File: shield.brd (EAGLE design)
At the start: 35.7 x 44.6 mm, 40 parts, among them Q1 BSS138, Q2 BSS138, Q3 BSS138, Q4 BSS138, Q5 BSS138, Q6 BSS138, Q7 BSS138, Q8 BSS138

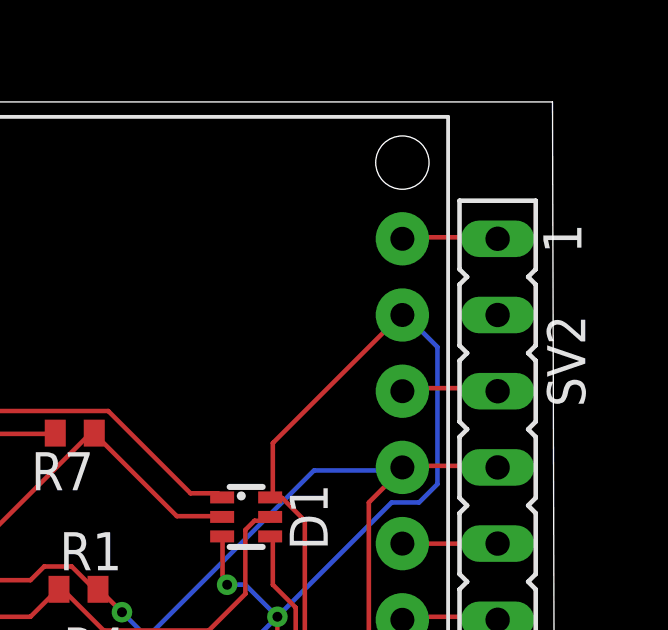
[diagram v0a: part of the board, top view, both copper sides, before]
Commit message: fixing ground line
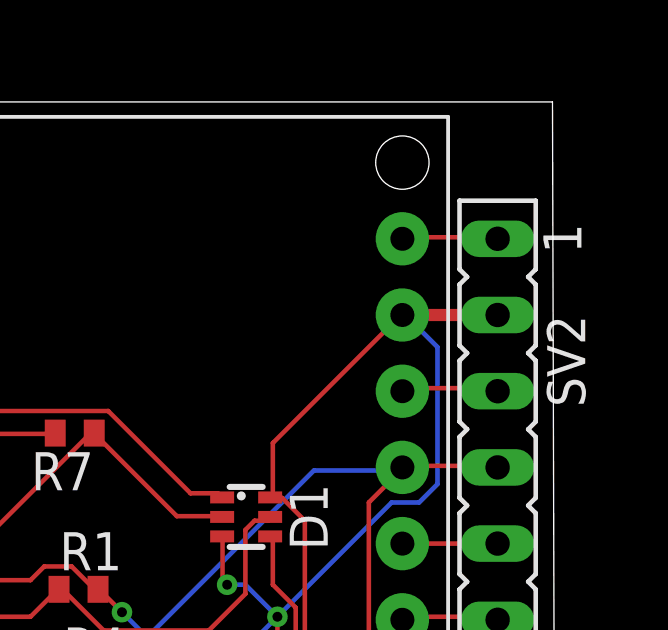
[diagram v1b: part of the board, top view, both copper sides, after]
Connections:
- removed net N$15: SV2.2
- net N$1: now also SV2.2
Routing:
- net N$1: track 76.5 -> 79.5 mm
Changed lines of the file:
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@@
 </signal>
 <signal name="N$1">
-<contactref element="U$1" pad="GND1"/>
 <contactref element="D1" pad="3"/>
 <contactref element="D1" pad="6"/>
@@
 <wire x1="43.2816" y1="45.72" x2="44.3484" y2="44.6532" width="0.1524" layer="16"/>
 <wire x1="39.0144" y1="33.3756" x2="38.9" y2="33.289" width="0.1524" layer="1"/>
-<wire x1="43.2816" y1="45.72" x2="43.18" y2="45.72" width="0.1524" layer="16"/>
 <wire x1="37.1856" y1="36.8808" x2="37.1856" y2="38.2524" width="0.1524" layer="1"/>
 <wire x1="37.338" y1="36.7284" x2="37.1856" y2="36.8808" width="0.1524" layer="1"/>
@@
 <wire x1="43.1292" y1="45.72" x2="38.862" y2="41.4528" width="0.1524" layer="1"/>
 <wire x1="38.862" y1="39.7764" x2="38.773" y2="39.639" width="0.1524" layer="1"/>
-<wire x1="43.1292" y1="45.72" x2="43.18" y2="45.72" width="0.1524" layer="1"/>
 <via x="39.0144" y="35.6616" extent="1-16" drill="0.3302"/>
 <via x="37.338" y="36.7284" extent="1-16" drill="0.3302"/>
 <via x="38.1" y="31.3944" extent="1-16" drill="0.3302"/>
 <via x="36.7284" y="25.146" extent="1-16" drill="0.3302"/>
+<contactref element="U$1" pad="GND1"/>
+<contactref element="SV2" pad="2"/>
+<wire x1="46.355" y1="45.72" x2="43.18" y2="45.72" width="0.4064" layer="1"/>
+<wire x1="43.1292" y1="45.72" x2="43.18" y2="45.72" width="0" layer="19" extent="1-1"/>
+<wire x1="43.2816" y1="45.72" x2="43.18" y2="45.72" width="0" layer="19" extent="16-16"/>
 </signal>
 <signal name="N$9">
@@
 <wire x1="43.2816" y1="43.2816" x2="43.18" y2="43.18" width="0.1524" layer="1"/>
 </signal>
-<signal name="N$15">
-<contactref element="SV2" pad="2"/>
-</signal>
 <signal name="N$16">

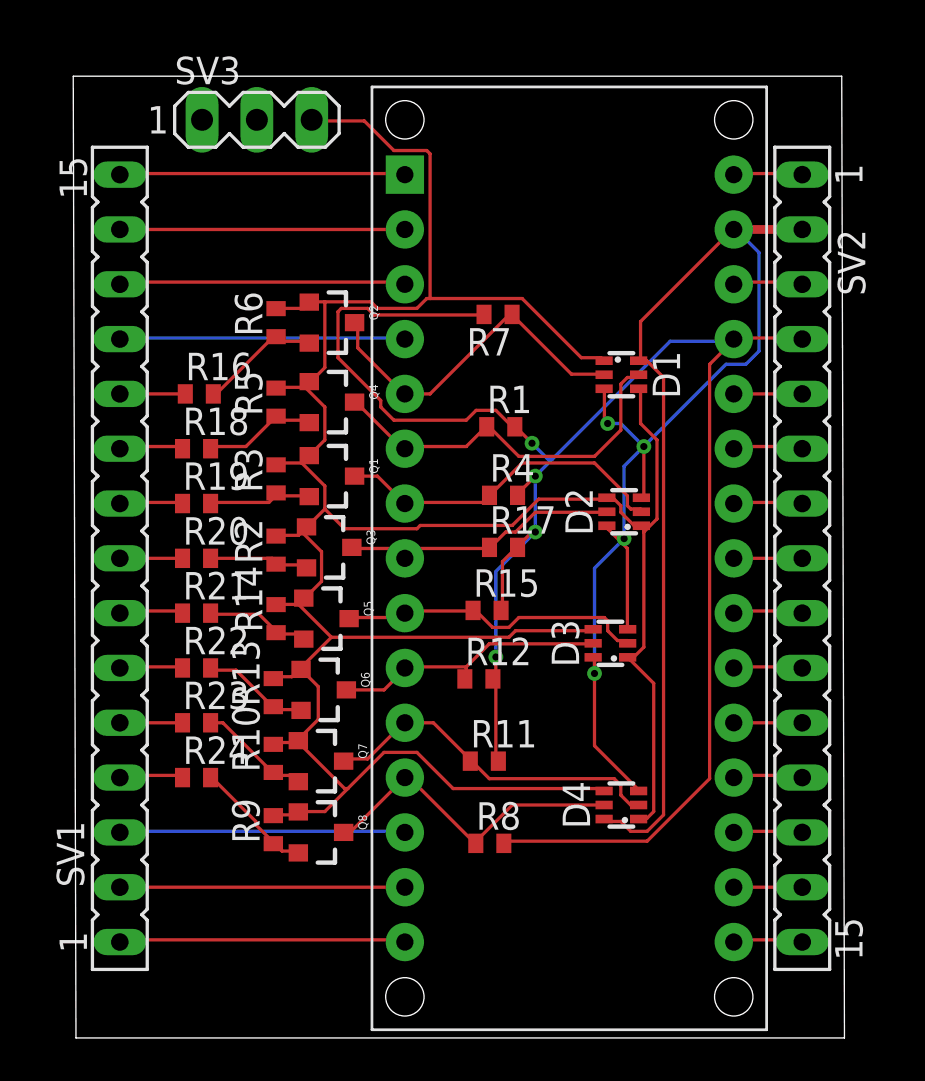
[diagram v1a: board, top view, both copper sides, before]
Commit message: optimizing board layout using reverse side for mounting
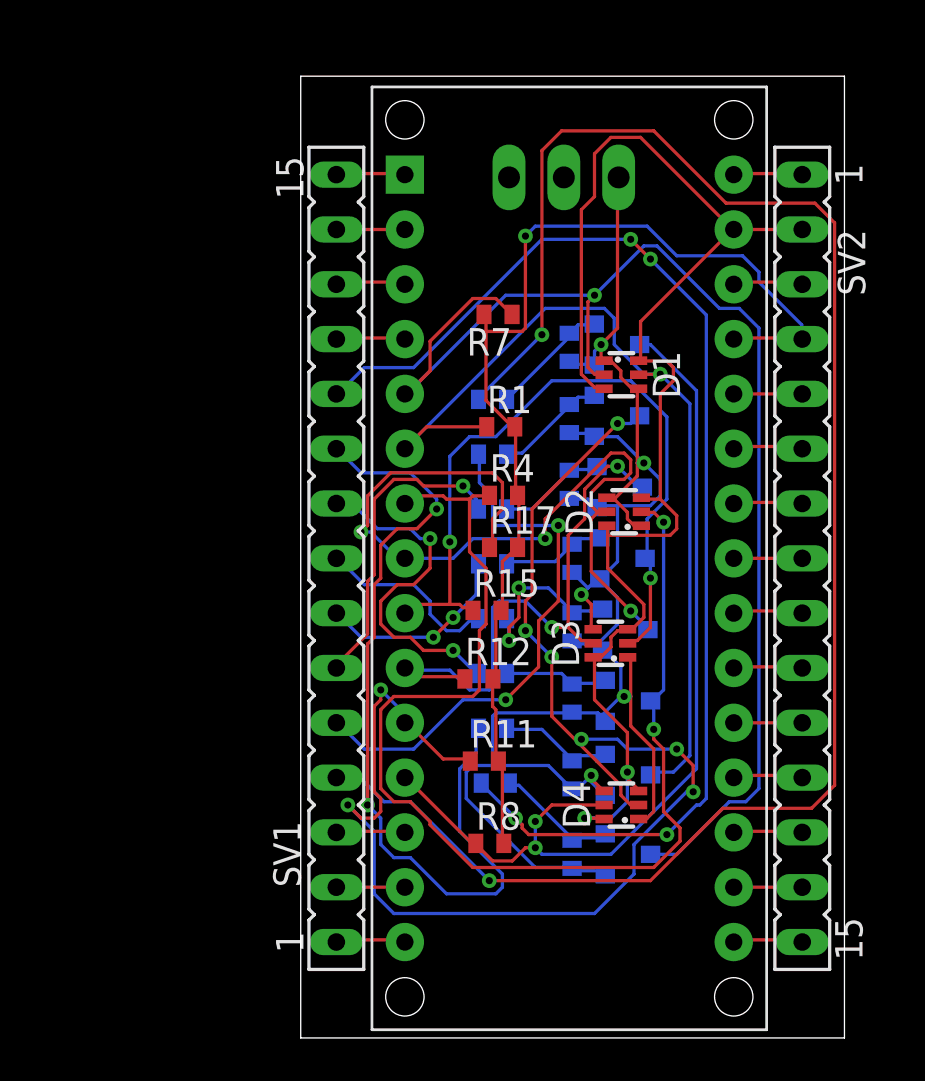
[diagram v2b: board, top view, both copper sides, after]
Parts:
- moved Q2 28.2 mm to (38.2, 16.8), flipped to the bottom, turned to 90 degrees
- moved R6 28.2 mm to (35.7, 16.8), flipped to the bottom, turned to 270 degrees
- moved Q8 26.4 mm to (37.7, 40.4), flipped to the bottom, turned to 90 degrees
- moved R9 26.2 mm to (35.6, 40.3), flipped to the bottom, turned to 270 degrees
- moved R16 22.7 mm to (32.1, 20.1), flipped to the bottom, turned to 180 degrees
- moved R24 22.3 mm to (32.0, 37.8), flipped to the bottom, turned to 180 degrees
- moved Q4 22.1 mm to (38.2, 20.4), flipped to the bottom, turned to 90 degrees
- moved R5 22.1 mm to (35.7, 20.4), flipped to the bottom, turned to 270 degrees
- moved Q7 21.1 mm to (37.7, 37.1), flipped to the bottom, turned to 90 degrees
- moved R10 20.9 mm to (35.6, 37.0), flipped to the bottom, turned to 270 degrees
- moved R18 18.9 mm to (32.0, 22.6), flipped to the bottom, turned to 180 degrees
- moved R23 18.5 mm to (32.0, 35.3), flipped to the bottom, turned to 180 degrees
- moved Q1 17.2 mm to (38.2, 23.9), flipped to the bottom, turned to 90 degrees
- moved R3 17.1 mm to (35.7, 24.0), flipped to the bottom, turned to 270 degrees
- moved R13 16.8 mm to (35.6, 33.9), flipped to the bottom, turned to 270 degrees
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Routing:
- net N$28: track 3.01 -> 81.4 mm, vias 0 -> 2
- net N$13: track 3.03 -> 56.2 mm, vias 0 -> 4
- net LV: track 135.5 -> 84.9 mm, vias 0 -> 5
- net HV8: track 16.3 -> 66.6 mm, vias 0 -> 8
- net HV2: track 16.2 -> 60.7 mm, vias 0 -> 1
- net HV4: track 15.8 -> 54.9 mm, vias 0 -> 2
- net HV: track 88.0 -> 51.3 mm, vias 4 -> 1
- net N$22: track 3.01 -> 39.0 mm, vias 0 -> 2
- net HV9: track 15.2 -> 42.9 mm, vias 0 -> 2
- net HV5: track 12.9 -> 38.5 mm, vias 0 -> 3
- net HV3: track 17.9 -> 42.2 mm, vias 0 -> 1
- net N$27: track 2.91 -> 24.9 mm, vias 0 -> 2
- net HV6: track 14.4 -> 34.2 mm, vias 0 -> 2
- net HV7: track 12.9 -> 27.1 mm, vias 0 -> 2
- net N$1: track 79.5 -> 65.4 mm, vias 4 -> 2
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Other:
- board size 35.7 x 44.6 mm -> 25.2 x 44.6 mm

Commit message: reducing size dramatically
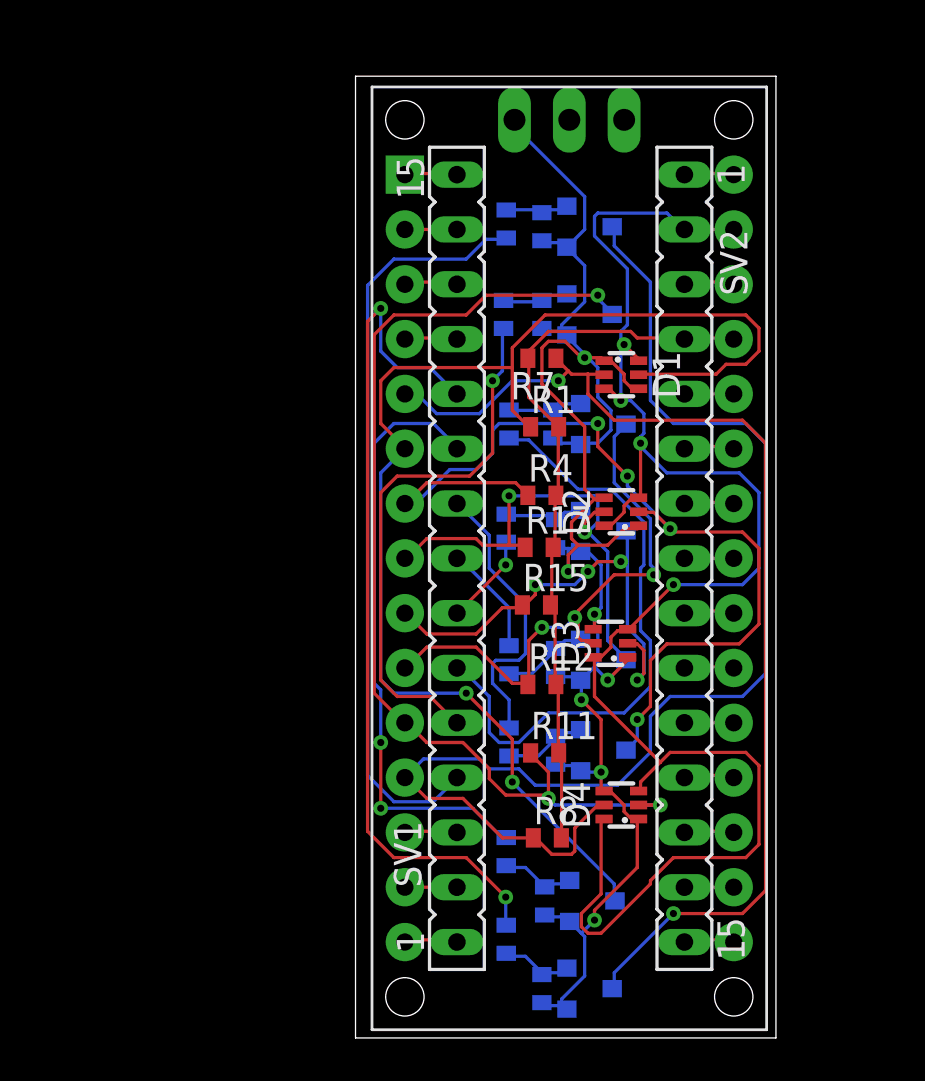
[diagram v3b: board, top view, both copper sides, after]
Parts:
- moved R24 8.15 mm to (32.6, 46.0), turned to 90 degrees
- moved R16 7.26 mm to (32.6, 12.8), turned to 270 degrees
- moved R23 6.50 mm to (32.5, 41.8), turned to 90 degrees
- moved Q2 6.47 mm to (36.4, 10.5)
- moved R6 6.38 mm to (34.3, 10.5)
- moved Q4 6.07 mm to (36.6, 14.6)
- moved R5 5.98 mm to (34.4, 14.6)
- moved R18 5.75 mm to (32.6, 16.9), turned to 270 degrees
- moved R9 5.73 mm to (34.3, 45.8)
- moved Q8 5.61 mm to (36.4, 45.8)
- moved SV1 5.59 mm to (30.4, 30.5)
- moved SV2 5.46 mm to (40.9, 30.5)
- moved R10 4.99 mm to (34.3, 41.8)
- moved Q7 4.87 mm to (36.4, 41.8)
- moved R22 4.01 mm to (32.8, 36.7), turned to 90 degrees
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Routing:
- net N$28: track 81.4 -> 35.2 mm, vias 2 -> 0
- net HV3: track 42.2 -> 61.3 mm, vias 1 -> 2
- net HV8: track 66.6 -> 47.9 mm, vias 8 -> 3
- net HV: track 51.3 -> 33.6 mm, vias 1 -> 0
- net N$13: track 56.2 -> 39.8 mm, vias 4 -> 2
- net HV5: track 38.5 -> 22.6 mm, vias 3 -> 2
- net HV9: track 42.9 -> 58.6 mm, vias 2 -> 0
- net N$26: track 14.7 -> 28.3 mm, vias 1 -> 0
- net N$1: track 65.4 -> 77.8 mm, vias 2 -> 4
- net HV6: track 34.2 -> 22.2 mm, vias 2 -> 4
- net HV4: track 54.9 -> 43.8 mm, vias 2 -> 4
- net N$22: track 39.0 -> 28.2 mm
- net HV2: track 60.7 -> 51.5 mm, vias 1 -> 2
- net N$25: track 9.25 -> 4.23 mm, vias 2 -> 1
- net LV5: track 8.15 -> 4.00 mm, vias 2 -> 0
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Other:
- board size 25.2 x 44.6 mm -> 19.5 x 44.6 mm
